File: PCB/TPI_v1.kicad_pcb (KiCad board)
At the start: 2 copper layers, 30 x 65 mm, 11 parts, among them J1 Raspberry pi zero w, J2 BME280, J3 BME280, U1 BMI160, U2 DS18B20

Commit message: PCB update
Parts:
- removed the ? at (171.0, 110.9)
- removed the ? at (148.0, 110.9)
- removed the ? at (171.0, 52.9)
- removed the ? at (148.0, 52.9)
- added ?: , , B.Cu at (171.0, 110.8)
- added ?: , , B.Cu at (148.0, 110.8)
- added ?: , , B.Cu at (171.0, 52.8)
- added ?: , , B.Cu at (148.0, 52.8)
- added C1: 100n, Capacitor_THT:C_Disc_D3.0mm_W1.6mm_P2.50mm, B.Cu at (171.1, 104.9)
- added G***: LOGO, Custom:Logo_TPI, F.Cu at (162.8, 108.0)
- added J4: MQ135, Connector_JST:JST_XH_B3B-XH-A_1x03_P2.50mm_Vertical, B.Cu at (163.8, 102.6)
- added J5: Buck, Connector_PinSocket_2.54mm:PinSocket_2x01_P2.54mm_Vertical, F.Cu at (156.2, 111.0)
- added R2: 10k, Resistor_THT:R_Axial_DIN0207_L6.3mm_D2.5mm_P7.62mm_Horizontal, B.Cu at (165.9, 77.6)
- added U3: MCP3008, Package_DIP:DIP-16_W7.62mm, F.Cu at (160.3, 95.5)
- added U4: DS18B20_2, Connector_JST:JST_XH_S3B-XH-A-1_1x03_P2.50mm_Horizontal, B.Cu at (172.0, 72.0)
- added U5: DS18B20_3, Connector_JST:JST_XH_S3B-XH-A-1_1x03_P2.50mm_Horizontal, B.Cu at (172.0, 60.3)
- added U6: DS18B20_4, Connector_JST:JST_XH_S3B-XH-A-1_1x03_P2.50mm_Horizontal, B.Cu at (172.0, 95.4)
- J2: footprint Connector_JST:JST_PH_S4B-PH-K_1x04_P2.00mm_Horizontal -> Connector_JST:JST_XH_S4B-XH-A-1_1x04_P2.50mm_Horizontal
- J3: value BME280 -> SIG2991; footprint Connector_JST:JST_PH_S4B-PH-K_1x04_P2.00mm_Horizontal -> Connector_JST:JST_XH_S2B-XH-A-1_1x02_P2.50mm_Horizontal
- U2: value DS18B20 -> DS18B20_1; footprint Connector_JST:JST_PH_S3B-PH-K_1x03_P2.00mm_Horizontal -> Connector_JST:JST_XH_S3B-XH-A-1_1x03_P2.50mm_Horizontal
- moved J3 56.5 mm to (164.1, 112.4), turned to 180 degrees
- moved J2 54.8 mm to (155.9, 53.1), turned to 0 degrees
- moved G*** 21.7 mm to (156.5, 86.9), turned to -90 degrees
- moved R1 21.2 mm to (165.7, 89.8), turned to -90 degrees
- moved U2 21.2 mm to (172.0, 83.7)
- moved U1 15.5 mm to (159.5, 66.7)
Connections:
- J1 pad 19: unconnected-(J1-GPIO10-Pad19) -> MOSI
- J1 pad 20: GND -> unconnected-(J1-GND-Pad20)
- J1 pad 21: unconnected-(J1-GPIO9-Pad21) -> MISO
- J1 pad 23: unconnected-(J1-GPIO11-Pad23) -> SCLK
- J1 pad 24: unconnected-(J1-GPIO8-Pad24) -> ~{CS}
- J1 pad 4: unconnected-(J1-5V-Pad4) -> +5V
- J3 pad 1: SCL -> ADC1
- J3 pad 2: SDA -> GND
- U1 pad 1: +3.3V -> +5V
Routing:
- net +5V: track 0.00 -> 207.6 mm
- net DQ: track 0.00 -> 122.0 mm
- net ADC1: track 0.00 -> 39.5 mm
- net SCL: track 0.00 -> 22.5 mm
- net SDA: track 0.00 -> 19.5 mm
- net ~{CS}: track 0.00 -> 11.4 mm
- net ADC0: track 0.00 -> 7.56 mm
- net SCLK: track 0.00 -> 4.24 mm
- net MOSI: track 0.00 -> 4.24 mm
- net MISO: track 0.00 -> 4.24 mm

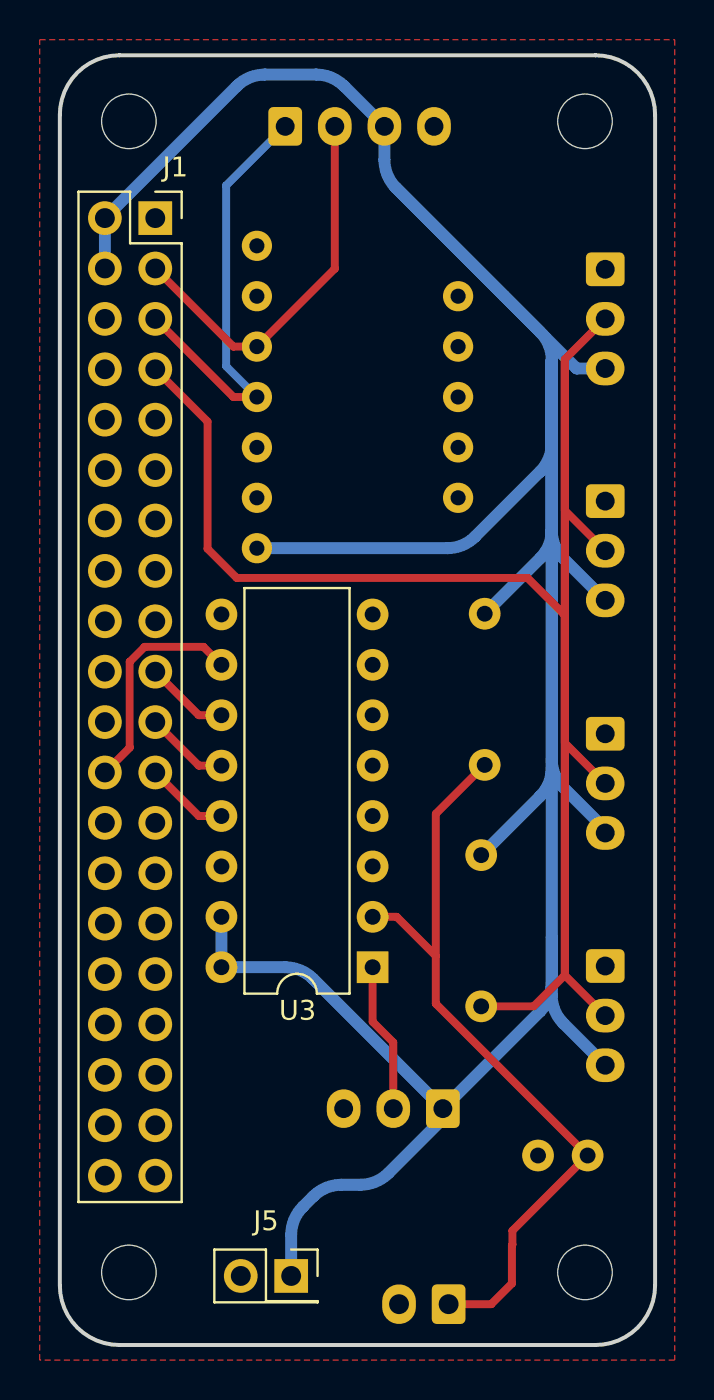
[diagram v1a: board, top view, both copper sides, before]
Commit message: PCB
Se cambio el voltaje del sensor BME280
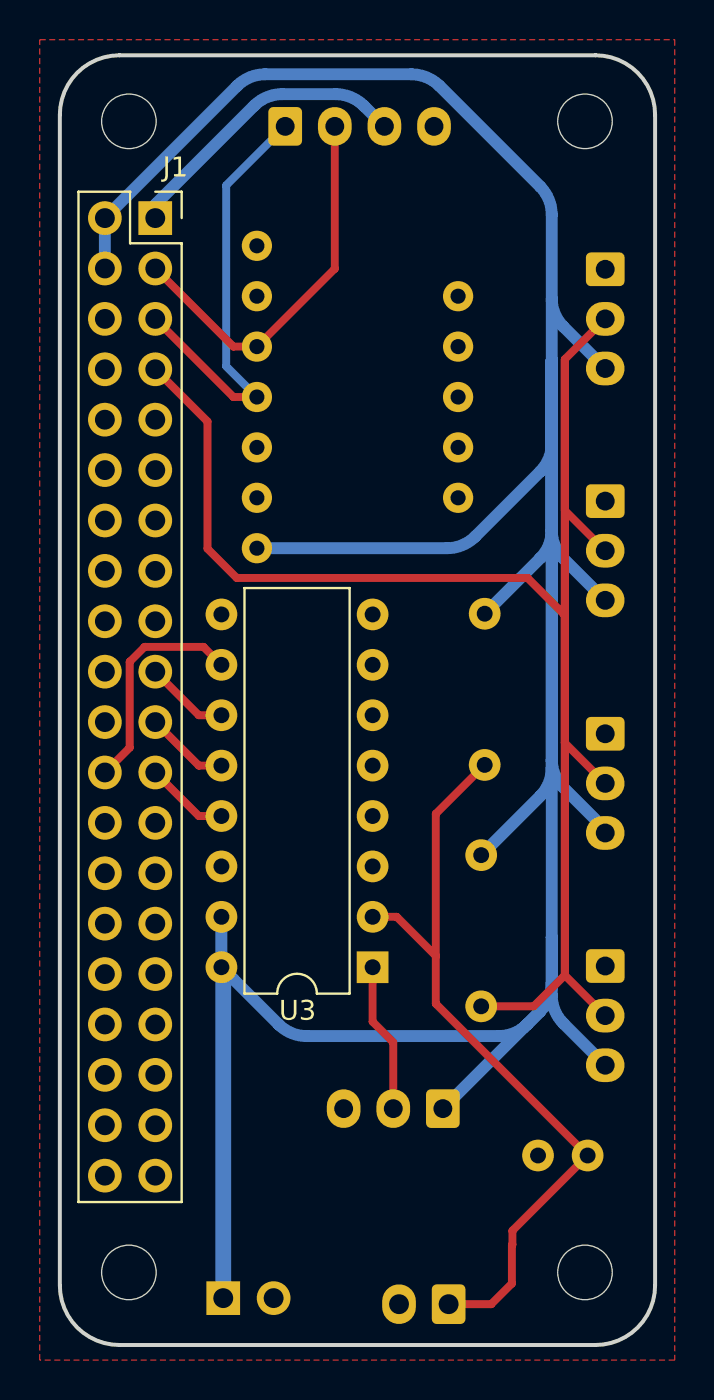
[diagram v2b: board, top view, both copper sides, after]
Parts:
- J5: moved to B.Cu
- moved J5 3.60 mm to (152.7, 112.1), turned to 180 degrees
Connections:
- J2 pad 3: +5V -> +3.3V
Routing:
- net +3.3V: track 0.08 -> 16.8 mm
- net +5V: track 207.6 -> 208.7 mm
